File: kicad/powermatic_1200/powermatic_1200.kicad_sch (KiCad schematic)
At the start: 34 parts

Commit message: PCB footprint and model work
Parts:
- removed K?: HMC-9B30-11-DS, symbol non_lcsc_parts:Non-LCSC/HMC-9B30-11-DS
- FH1: renamed from FH?; footprint (none) -> Controls:RM25030-3SR_Front; Package (none) -> DIN rail fuse holder
- H1: renamed from H?; footprint (none) -> Controls_Review:XB4BVB1_LeftWall; Package (none) -> 22 mm panel mount
- J1: renamed from J?; footprint (none) -> Controls_Review:T4171310004-001_LeftWall
- KF1, KH1, KL1, KR1, KS1: renamed from K?; footprint (none) -> Controls:HMC-9B30-11-DS_Front; Package (none) -> DIN rail contactor
- MI1: renamed from MI?; footprint (none) -> Controls:HMX1-MI_Front; Package (none) -> Contactor interlock
- OL1, OL2: renamed from OL?; footprint (none) -> Controls:HTOR32-6-S_Front; Package (none) -> Contactor-mounted overload
- PS1: renamed from PS?; footprint (none) -> Controls:NDR-240-24_Front; Package (none) -> DIN rail 63 x 125.2 x 113.5 mm
- Q1: renamed from Q?; footprint (none) -> Controls:FAZ-D4-2-NA-L_Front; Package (none) -> 35 mm DIN rail
- SP1, SP2, SP3, SP4, SP5: renamed from SP?; footprint (none) -> Controls:HMX1-SSVRC-DC_Front; Package (none) -> Contactor accessory
- SW1: renamed from SW?; footprint (none) -> Controls_Review:22013003_LeftWall; Package (none) -> Panel disconnect
- TB1: renamed from J?; footprint (none) -> Controls:KN-T12GRY-25_Front
- gave numbers to parts that had none: 4

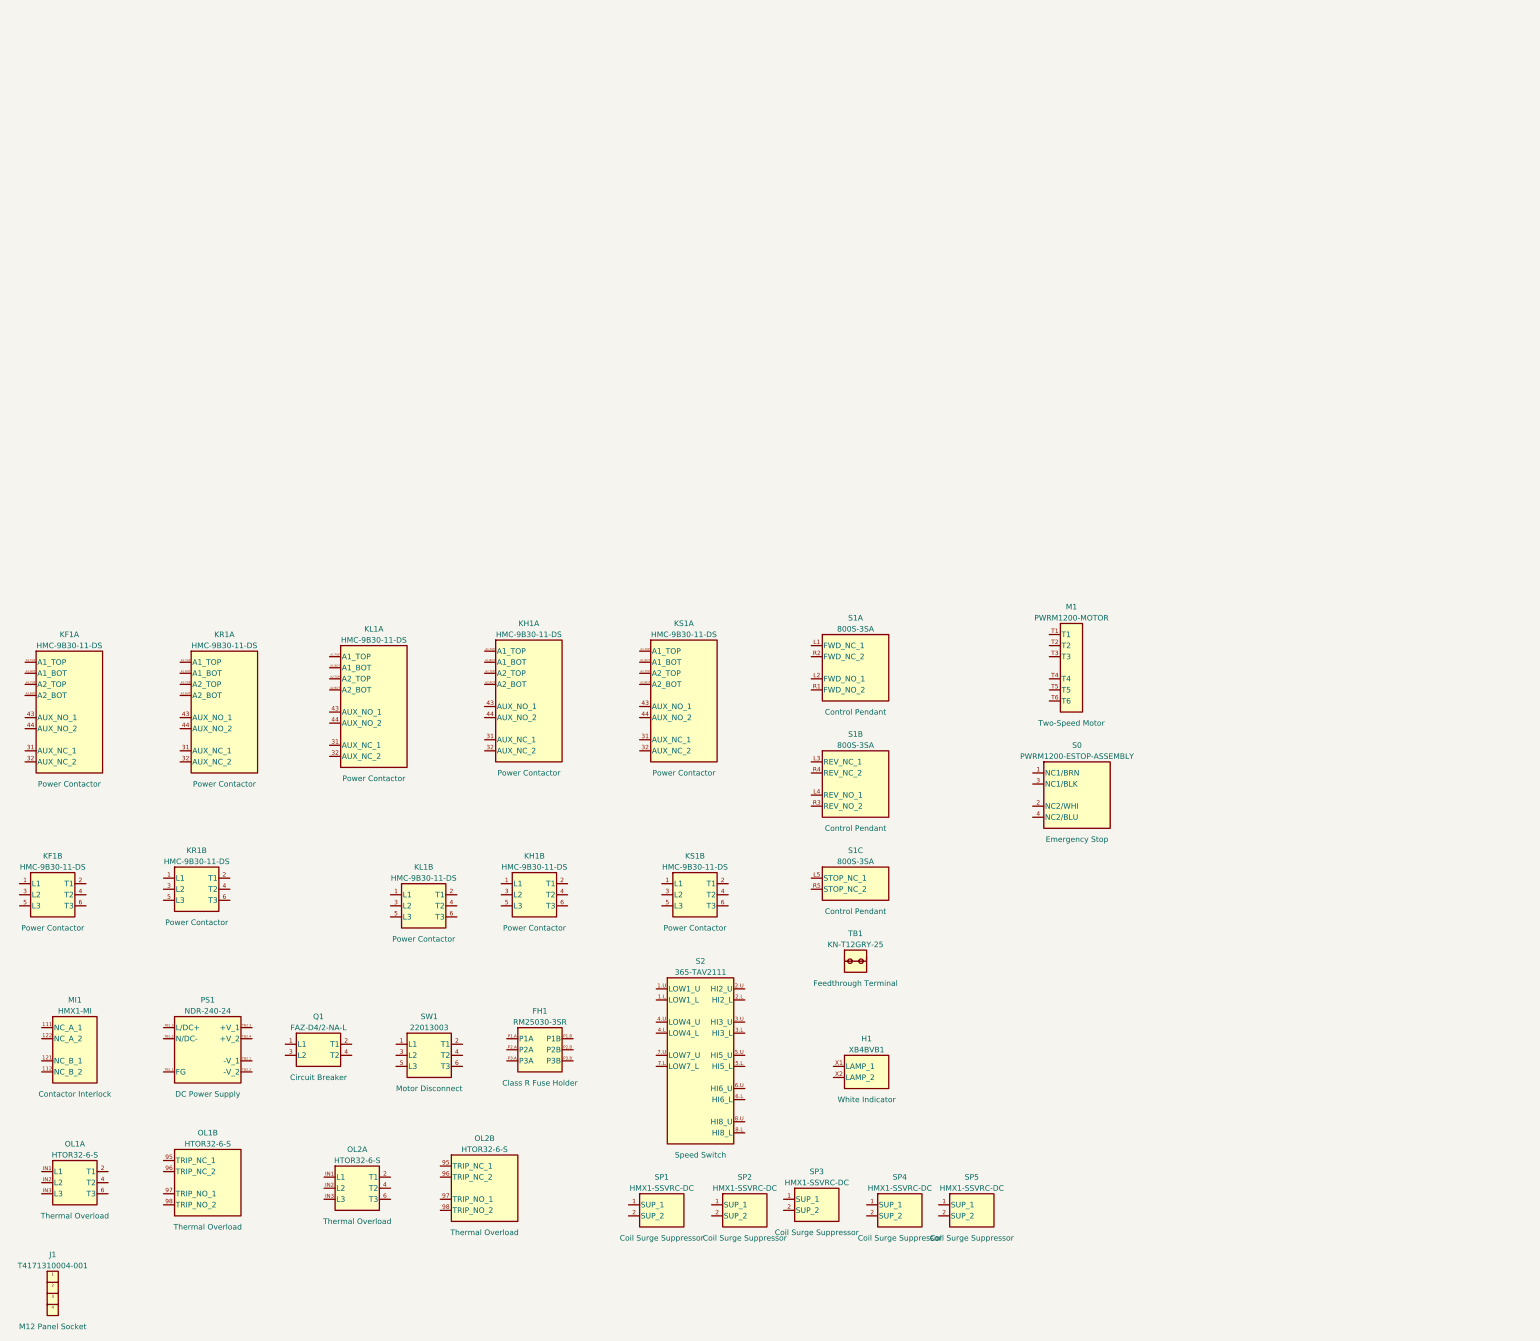
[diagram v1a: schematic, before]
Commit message: Advance motor-control wiring and use shared Controls assets
Save the current power, stop-chain, direction-holding, and speed-coil wiring checkpoint. Simplify contactor references, use the BACO disconnect, and migrate project-local Controls assets to _parts with updated geometry tooling and project settings.
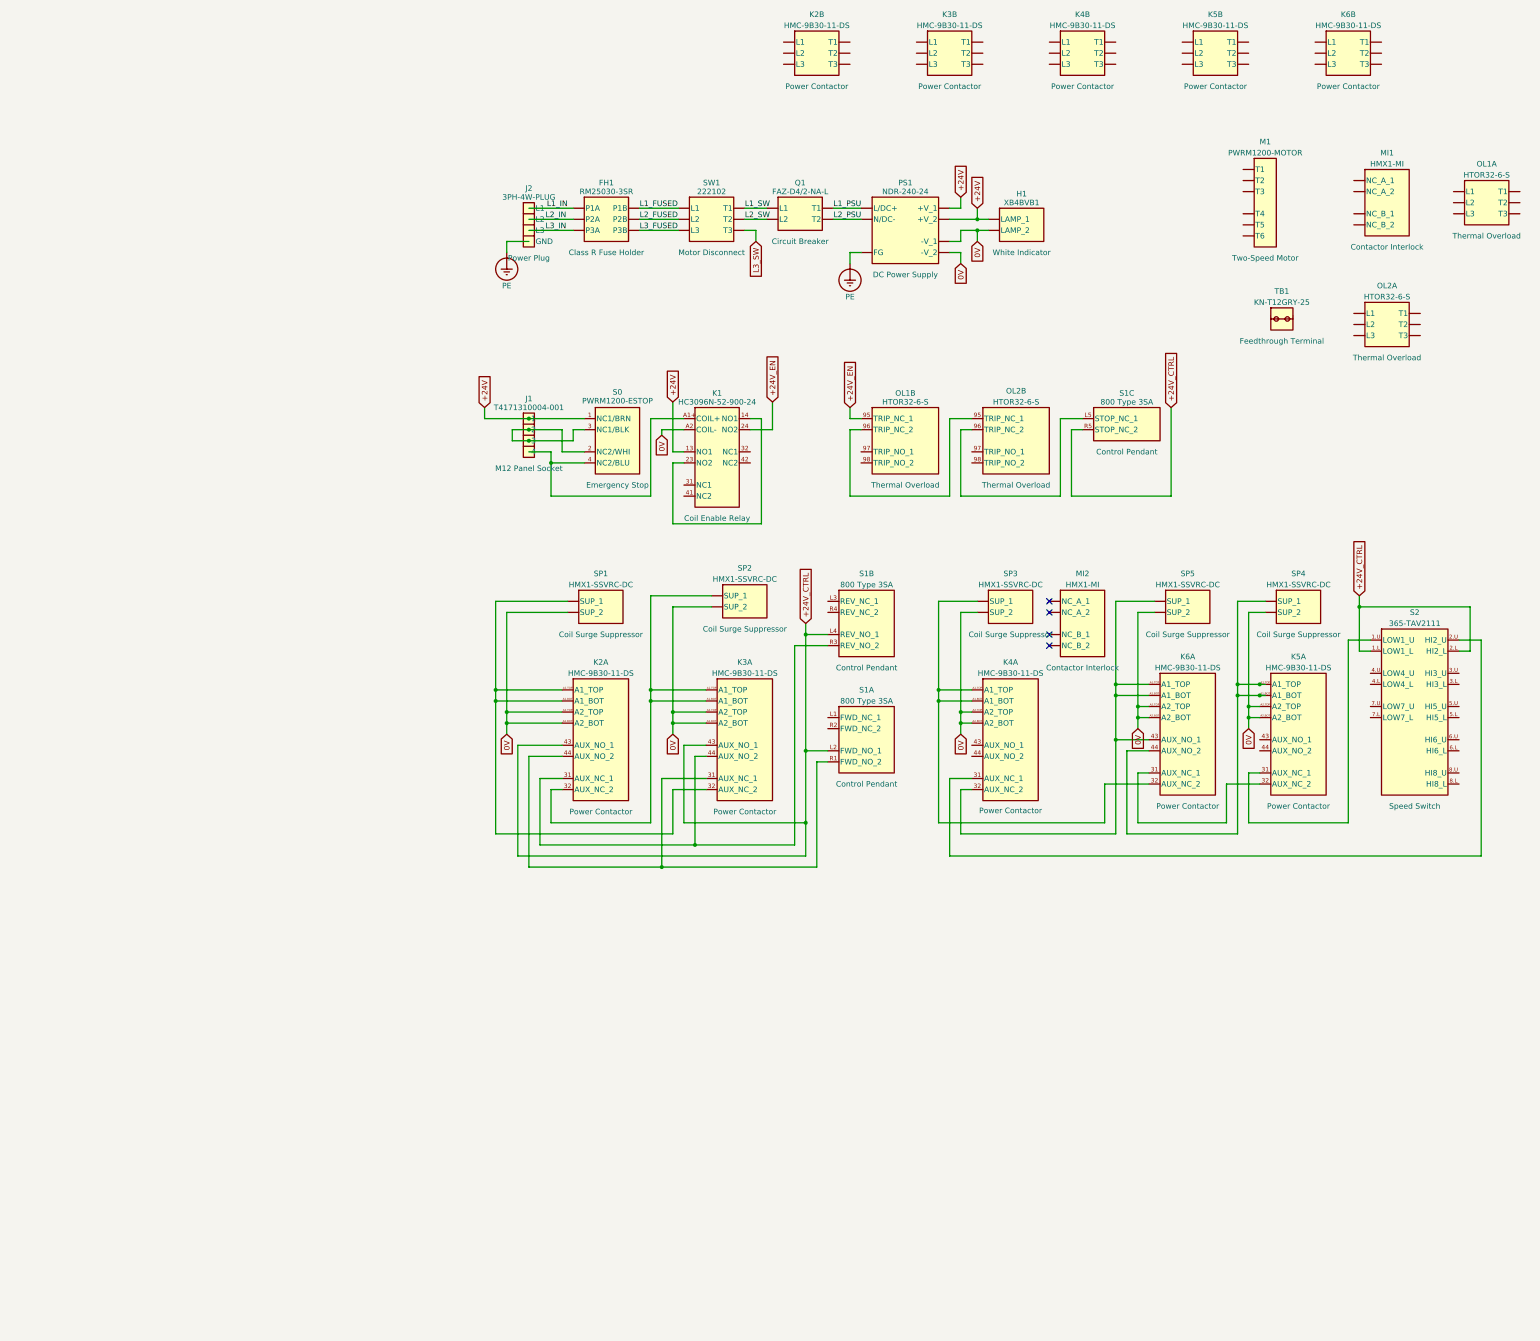
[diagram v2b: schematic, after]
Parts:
- added J2: 3PH-4W-PLUG, symbol Controls:3PH-4W-PLUG
- added K1: HC3096N-52-900-24, symbol non_lcsc_parts:Non-LCSC/HC3096N-52-900-24
- added MI2: HMX1-MI, Controls:HMX1-MI_Front, symbol non_lcsc_parts:Non-LCSC/HMX1-MI
- H1: footprint Controls_Review:XB4BVB1_LeftWall -> Controls:XB4BVB1_LeftWall
- J1: footprint Controls_Review:T4171310004-001_LeftWall -> Controls:T4171310004-001_LeftWall
- S0: value PWRM1200-ESTOP-ASSEMBLY -> PWRM1200-ESTOP
- S1: value 800S-3SA -> 800 Type 3SA; MPN 800S-3SA -> (none)
- SW1: value 22013003 -> 222102; footprint Controls_Review:22013003_LeftWall -> Controls:222102_LeftWall; symbol non_lcsc_parts:Non-LCSC/22013003 -> non_lcsc_parts:Non-LCSC/222102; MPN 22013003 -> 222102; Manufacturer Socomec -> BACO; Part ID 22013003 -> 222102; Supplier AutomationDirect -> McMaster-Carr; Supplier PN 22013003 -> 6759K211; inventory 0 -> 1
- renumbered KF1 to K2, KR1 to K3, KL1 to K4, KH1 to K5, KS1 to K6
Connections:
- net +24V_EN: now reaches OL1.95 (TRIP_NC_1)
- net +24V_EN: now also K1.24 (NO2)
- net at OL1.96 (TRIP_NC_2): now also OL2.95 (TRIP_NC_1)
- net at SP4.1 (SUP_1): now also K5.A1.BOT (A1_BOT), K5.A1.TOP (A1_TOP), K6.44 (AUX_NO_2)
- net 0V: now reaches SP4.2 (SUP_2)
- net 0V: now also H1.X2 (LAMP_2), K2.A2.BOT (A2_BOT), K2.A2.TOP (A2_TOP), K3.A2.BOT (A2_BOT), K3.A2.TOP (A2_TOP), K4.A2.BOT (A2_BOT), K4.A2.TOP (A2_TOP), K5.A2.BOT (A2_BOT), K5.A2.TOP (A2_TOP), K6.A2.BOT (A2_BOT), K6.A2.TOP (A2_TOP), PS1.TB2.1 (-V_1), PS1.TB2.2 (-V_2), SP1.2 (SUP_2), SP2.2 (SUP_2), SP3.2 (SUP_2), SP5.2 (SUP_2), K1.A2 (COIL-)
- net at K5.31 (AUX_NC_1): now also S2.1.U (LOW1_U)
- net at K5.32 (AUX_NC_2): now also K6.31 (AUX_NC_1)
- net at K3.31 (AUX_NC_1): now also K2.44 (AUX_NO_2), S1.R1 (FWD_NO_2)
- net at K3.32 (AUX_NC_2): now also K2.A1.BOT (A1_BOT), K2.A1.TOP (A1_TOP), SP1.1 (SUP_1)
- net +24V_CTRL: now reaches K3.43 (AUX_NO_1)
- net +24V_CTRL: now also K2.43 (AUX_NO_1), S1.L2 (FWD_NO_1), S1.L4 (REV_NO_1), S1.R5 (STOP_NC_2), S2.1.L (LOW1_L), S2.2.L (HI2_L)
- net at K3.44 (AUX_NO_2): now also K2.31 (AUX_NC_1), S1.R3 (REV_NO_2)
- net at K3.A1.BOT (A1_BOT): now also K2.32 (AUX_NC_2), K3.A1.TOP (A1_TOP), SP2.1 (SUP_1)
- net +24V: now reaches S0.1 (NC1/BRN)
- net +24V: now also H1.X1 (LAMP_1), J1.1, PS1.TB2.3 (+V_1), PS1.TB2.4 (+V_2), K1.13 (NO1)
- net at S0.2 (NC2/WHI): now also J1.2, J1.3, S0.3 (NC1/BLK)
- net at S0.4 (NC2/BLU): now also J1.4, K1.A1+ (COIL+)
- net L1_IN: now reaches FH1.P1.A (P1A)
- net L1_IN: now also J2.X (L1)
- net L1_FUSED: now reaches FH1.P1.B (P1B)
- net L1_FUSED: now also SW1.1 (L1)
- net L2_IN: now reaches FH1.P2.A (P2A)
- net L2_IN: now also J2.Y (L2)
- net L2_FUSED: now reaches FH1.P2.B (P2B)
- net L2_FUSED: now also SW1.3 (L2)
- net L3_IN: now reaches FH1.P3.A (P3A)
- net L3_IN: now also J2.Z (L3)
- net L3_FUSED: now reaches FH1.P3.B (P3B)
- net L3_FUSED: now also SW1.5 (L3)
- net at SP3.1 (SUP_1): now also K4.A1.BOT (A1_BOT), K4.A1.TOP (A1_TOP), K6.32 (AUX_NC_2)
- net at K6.43 (AUX_NO_1): now also K4.32 (AUX_NC_2), K6.A1.BOT (A1_BOT), K6.A1.TOP (A1_TOP), SP5.1 (SUP_1)
- net PE: now reaches PS1.TB1.1 (FG)
- net PE: now also J2.G (GND)
- net L2_PSU: now reaches PS1.TB1.2 (N/DC-)
- net L2_PSU: now also Q1.4 (T2)
- net L1_PSU: now reaches PS1.TB1.3 (L/DC+)
- net L1_PSU: now also Q1.2 (T1)
- net L1_SW: now reaches Q1.1 (L1)
- net L1_SW: now also SW1.2 (T1)
- net L2_SW: now reaches Q1.3 (L2)
- net L2_SW: now also SW1.4 (T2)
- net at OL2.96 (TRIP_NC_2): now also S1.L5 (STOP_NC_1)
- net at K4.31 (AUX_NC_1): now also S2.2.U (HI2_U)
- net L3_SW: now reaches SW1.6 (T3)
- new net: K1.14 (NO1), K1.23 (NO2)
- no-connect marks 0 -> 4
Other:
- moved on the sheet: J1, K2A, K3A, K4A, K5A, K6A, OL1B, OL2B, S0, S1A, S1B, S1C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
